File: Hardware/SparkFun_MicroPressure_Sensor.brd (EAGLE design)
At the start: 25.4 x 25.4 mm, 43 parts, among them J1 Qwiic, J2 Qwiic, U1 MPR_Pressure_Sensor

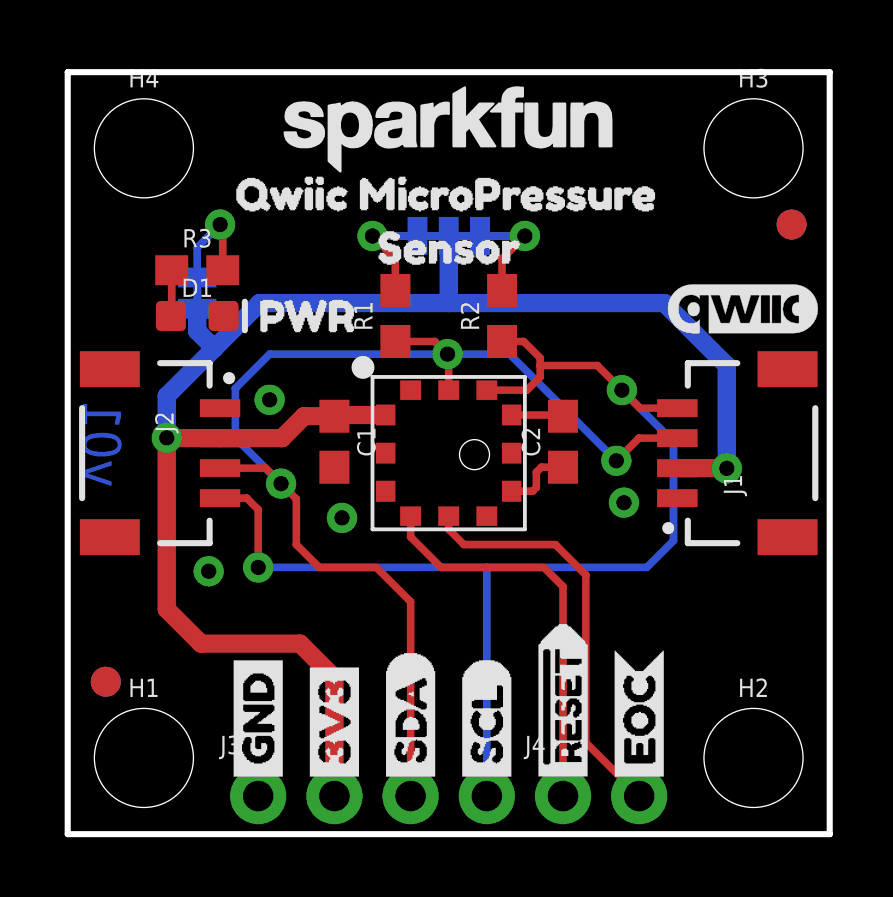
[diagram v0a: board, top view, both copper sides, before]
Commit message: v01 Update
- Added address to schematic, and pcb files
- Rerouted 3.3V trace for better ground pour.
- Updated MPR footprint silk
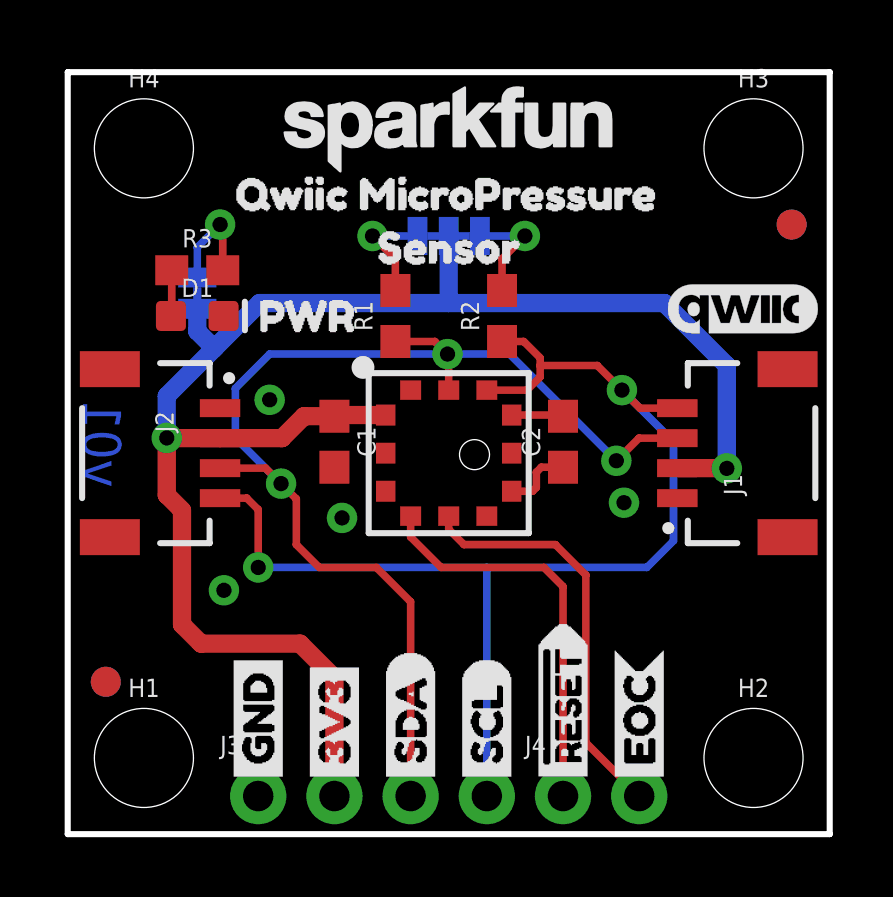
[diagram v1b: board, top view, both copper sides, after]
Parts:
- added U$17: (no value), buzzard_labels(3):ADR_#_0X180
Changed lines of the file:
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@@
 <layer number="37" name="tTest" color="7" fill="1" visible="no" active="yes"/>
 <layer number="38" name="bTest" color="7" fill="1" visible="no" active="yes"/>
-<layer number="39" name="tKeepout" color="4" fill="11" visible="yes" active="yes"/>
+<layer number="39" name="tKeepout" color="4" fill="11" visible="no" active="yes"/>
 <layer number="40" name="bKeepout" color="1" fill="11" visible="no" active="yes"/>
 <layer number="41" name="tRestrict" color="4" fill="10" visible="no" active="yes"/>
@@
 <layer number="45" name="Holes" color="7" fill="1" visible="yes" active="yes"/>
 <layer number="46" name="Milling" color="3" fill="1" visible="no" active="yes"/>
-<layer number="47" name="Measures" color="7" fill="1" visible="yes" active="yes"/>
+<layer number="47" name="Measures" color="7" fill="1" visible="no" active="yes"/>
 <layer number="48" name="Document" color="7" fill="1" visible="no" active="yes"/>
 <layer number="49" name="Reference" color="7" fill="1" visible="no" active="yes"/>
 <layer number="50" name="dxf" color="7" fill="1" visible="no" active="yes"/>
 <layer number="51" name="tDocu" color="6" fill="1" visible="yes" active="yes"/>
-<layer number="52" name="bDocu" color="7" fill="1" visible="yes" active="yes"/>
+<layer number="52" name="bDocu" color="7" fill="1" visible="no" active="yes"/>
 <layer number="91" name="Nets" color="2" fill="1" visible="no" active="no"/>
 <layer number="92" name="Busses" color="1" fill="1" visible="no" active="no"/>
@@
 </element>
 <element name="U1" library="MPR_Temp" package="MPRL" value="MPR_Pressure_Sensor" x="12.7" y="12.7" smashed="yes" rot="R180">
-<attribute name="PROD_ID" value="SEN-" x="-17.78" y="25.4" size="1.778" layer="27" rot="R180" display="off"/>
+<attribute name="PROD_ID" value="IC-15069" x="-17.78" y="25.4" size="1.778" layer="27" rot="R180" display="off"/>
 </element>
 <element name="H1" library="SparkFun-Hardware" package="STAND-OFF" value="STAND-OFF" x="2.54" y="2.54" smashed="yes">
@@
 <element name="U$19" library="SparkFun-Aesthetics" package="SFE_LOGO_NAME_.1" value="" x="12.7" y="23.495" smashed="yes"/>
 <element name="U$16" library="buzzard_labels(2)" package="QWIIC_MICROPRESSURE0" value="" x="4.699" y="21.336" smashed="yes"/>
+<element name="U$17" library="buzzard_labels(3)" package="ADR_#_0X180" value="" x="17.145" y="7.747" smashed="yes" rot="MR0"/>
 </elements>
 <signals>
@@
 <vertex x="25.4" y="0"/>
 </polygon>
-<via x="4.699" y="8.763" extent="1-16" drill="0.508"/>
+<via x="5.207" y="8.128" extent="1-16" drill="0.508"/>
 <contactref element="D1" pad="C"/>
 </signal>
@@
 <wire x1="8.89" y1="5.207" x2="7.747" y2="6.35" width="0.6096" layer="1"/>
 <wire x1="7.747" y1="6.35" x2="4.445" y2="6.35" width="0.6096" layer="1"/>
-<wire x1="4.445" y1="6.35" x2="3.302" y2="7.493" width="0.6096" layer="1"/>
-<wire x1="3.302" y1="7.493" x2="3.302" y2="13.208" width="0.6096" layer="1"/>
+<wire x1="4.445" y1="6.35" x2="3.81" y2="6.985" width="0.6096" layer="1"/>
+<wire x1="3.81" y1="10.795" x2="3.302" y2="11.303" width="0.6096" layer="1"/>
+<wire x1="3.302" y1="11.303" x2="3.302" y2="13.208" width="0.6096" layer="1"/>
+<wire x1="3.81" y1="10.795" x2="3.81" y2="6.985" width="0.6096" layer="1"/>
 <contactref element="PWR" pad="1"/>
 <wire x1="4.318" y1="17.5133" x2="4.318" y2="16.764" width="0.6096" layer="16"/>

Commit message: V10
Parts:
- removed U$17: (no value), buzzard_labels(3):ADR_#_0X180
- added R4: 2.2k, SparkFun-Resistors:0603
- FD1, FD2, FD3, FD4: value FIDUCIAL1X2 -> FIDUCIALUFIDUCIAL; device SparkFun-Aesthetics:FIDUCIAL-1X2 -> SparkFun-Aesthetics:FIDUCIAL-MICRO
- R1, R2: value 4.7k -> 2.2k
- U$9: device buzzard_labels:I2C6 -> buzzard_labels(4):I#C0
- U1: value MPR_Pressure_Sensor -> MPR Series; device MPR_Temp:MPRL -> SparkFun-Sensors:MPR_SERIES_PRESSURE_I2C
- moved FD1 4.49 mm to (0.64, 0.64)
- moved FD2 4.49 mm to (0.64, 0.64)
- moved FD3 4.49 mm to (24.8, 24.8)
- moved FD4 4.49 mm to (24.8, 24.8)
- moved U$9 0.13 mm to (14.6, 21.7)
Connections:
- new net MISO: U1.7
- new net SS: U1.1
- net !RESET: now also R4.2
- net 3.3V: now also R4.1
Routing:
- net 3.3V: track 54.9 -> 60.8 mm, vias 2 -> 4
- net SDA: track 39.5 -> 38.4 mm
- net N$4: track 3.63 -> 4.54 mm
- net N$3: track 3.63 -> 4.54 mm
- net !RESET: track 13.4 -> 14.3 mm
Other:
- board text added: "v10"
- board text removed: "v01"
